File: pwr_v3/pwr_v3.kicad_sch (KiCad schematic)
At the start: 23 parts, among them J5 530470610, M1 Conn_02x03_Counter_Clockwise, M2 Conn_02x03_Counter_Clockwise, M3 Conn_02x03_Counter_Clockwise, M4 Conn_02x03_Counter_Clockwise, Q1 BUK9832-55A, SW1 SW_SPST

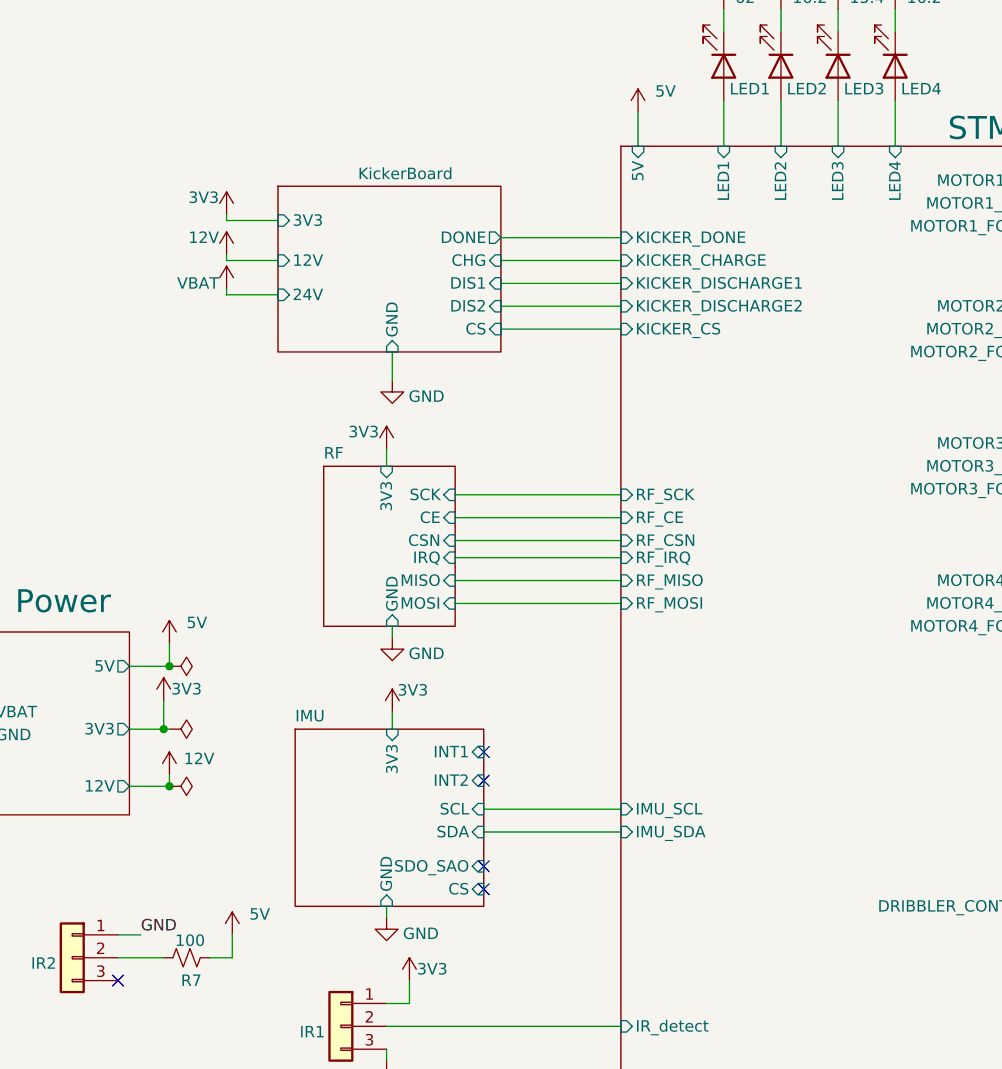
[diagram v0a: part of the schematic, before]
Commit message: Schematic and layout updated
Sch - Unwanted global labels removed from IMU, added new kicker labels, changed kicker connector footprint.
Layout - Updated kicker and encoder positions, routing updated.
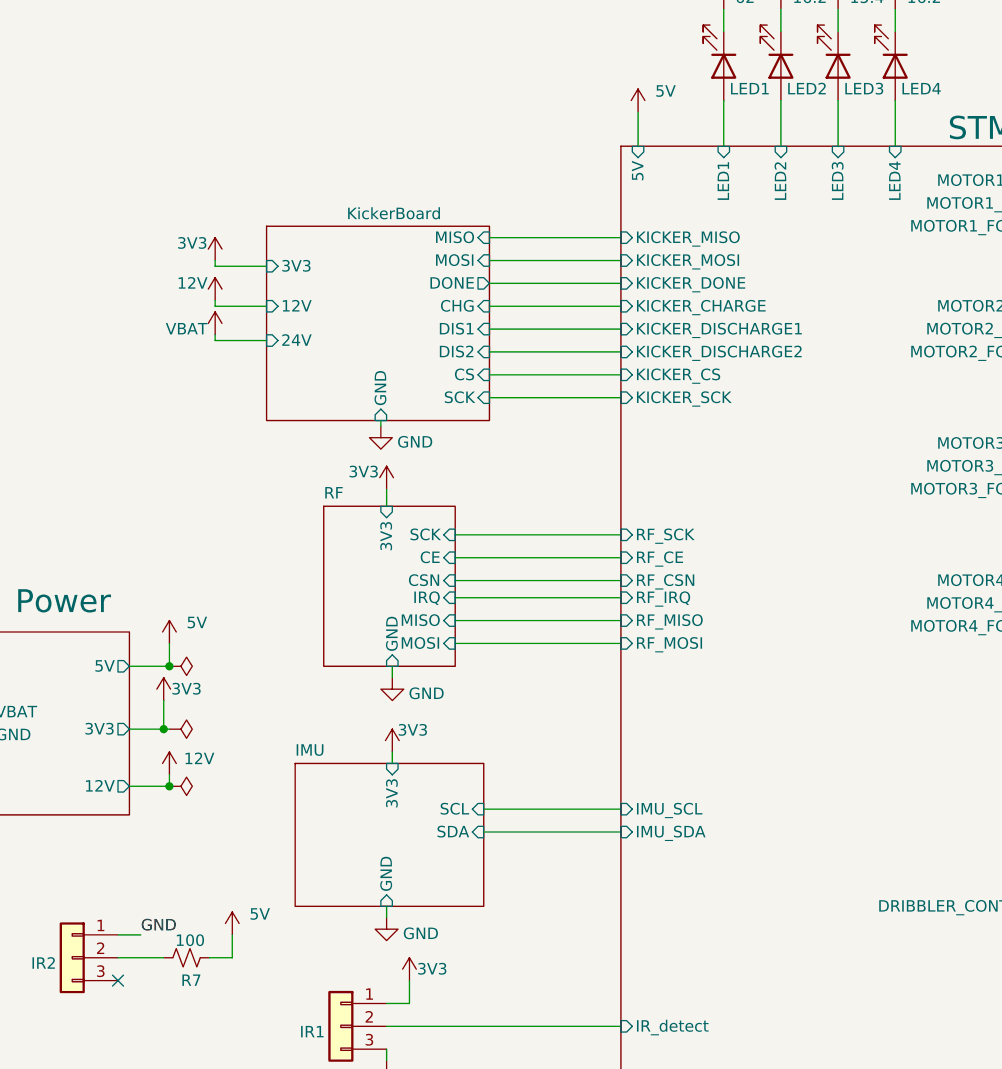
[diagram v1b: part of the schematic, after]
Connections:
- no-connect marks 5 -> 1
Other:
- sheet IMU ports: added none; removed CS, INT1, INT2, SDO_SAO
- sheet KickerBoard ports: added MISO, MOSI, SCK; removed none
- sheet STM32 ports: added KICKER_MISO, KICKER_MOSI, KICKER_SCK; removed none

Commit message: Finalized files
Final files used for fabrication. Docs and Images added for easy view.
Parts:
- added IR_1: Conn_01x02, Connector_PinHeader_2.54mm:PinHeader_1x02_P2.54mm_Vertical, symbol Connector_Generic:Conn_01x02
- J5: now left out of the parts list
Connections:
- net 3V3: now also IR1.3 (Pin_3); no longer IR1.1 (Pin_1)
- net 5V: now also J5.5 (Pin_5), J5.6 (Pin_6), IR_1.2 (Pin_2); no longer J5.1 (Pin_1), J5.2 (Pin_2), R7.1
- net GND: now also IR1.1 (Pin_1), IR2.3 (Pin_3), J5.1 (Pin_1), J5.2 (Pin_2); no longer IR1.3 (Pin_3), IR2.1 (Pin_1), J5.5 (Pin_5), J5.6 (Pin_6)
- net STM32/ENC_SCL: now also J5.3 (Pin_3); no longer J5.4 (Pin_4)
- net STM32/ENC_SDA: now also J5.4 (Pin_4); no longer J5.3 (Pin_3)
- new net: IR_1.1 (Pin_1), R7.1
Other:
- note added: "Encoder-counter PCB"
- note added: "Main changes: - New encoder connector added - IR conn connections changed - Kicker conn connections and placement updated"
- note added: "Motordriver PCB"
- note added: "Powerboard"
- note added: "The IR transmitter can be controlled through IR_1 connector by adding or removing the shunt jumper"
- note removed: "Main changes: Motor driver is on a separate board. Fixed nRF connector pin issue. Kicker and battery connectors on bottom side. Dribbler motor circuit updated Added LEDs and buzzer."
- moved on the sheet: BAT1, BUZZER1, BZ1, D4, DRIBBLER1, IR1, IR2, J5, LED1, LED2, LED3, LED4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
